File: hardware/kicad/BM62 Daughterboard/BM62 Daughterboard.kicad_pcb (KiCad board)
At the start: 2 copper layers, 29 x 34.5 mm, 10 parts, among them J1 Conn_2x4, SW1 SW_DIP_x03, U1 BM62

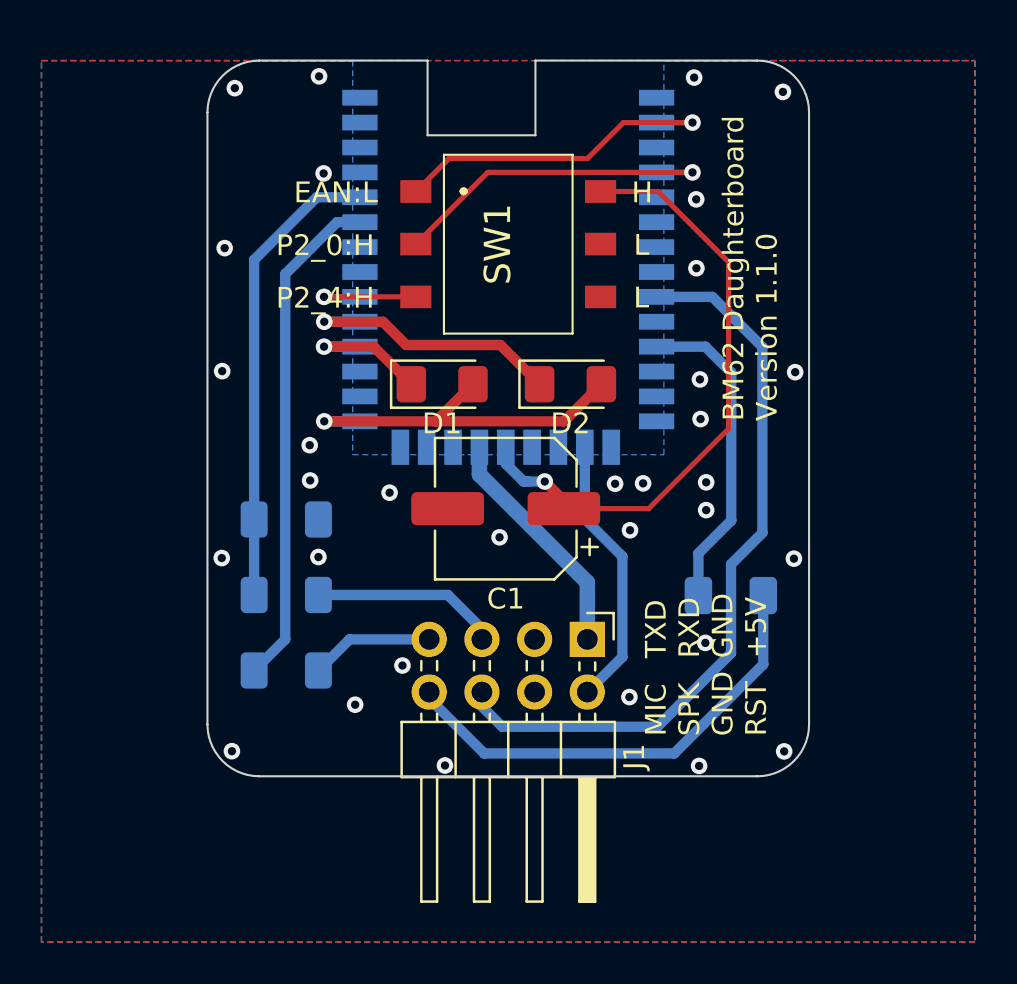
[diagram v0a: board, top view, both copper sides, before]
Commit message: Align some components better on the BM62 Daughterboard PCB
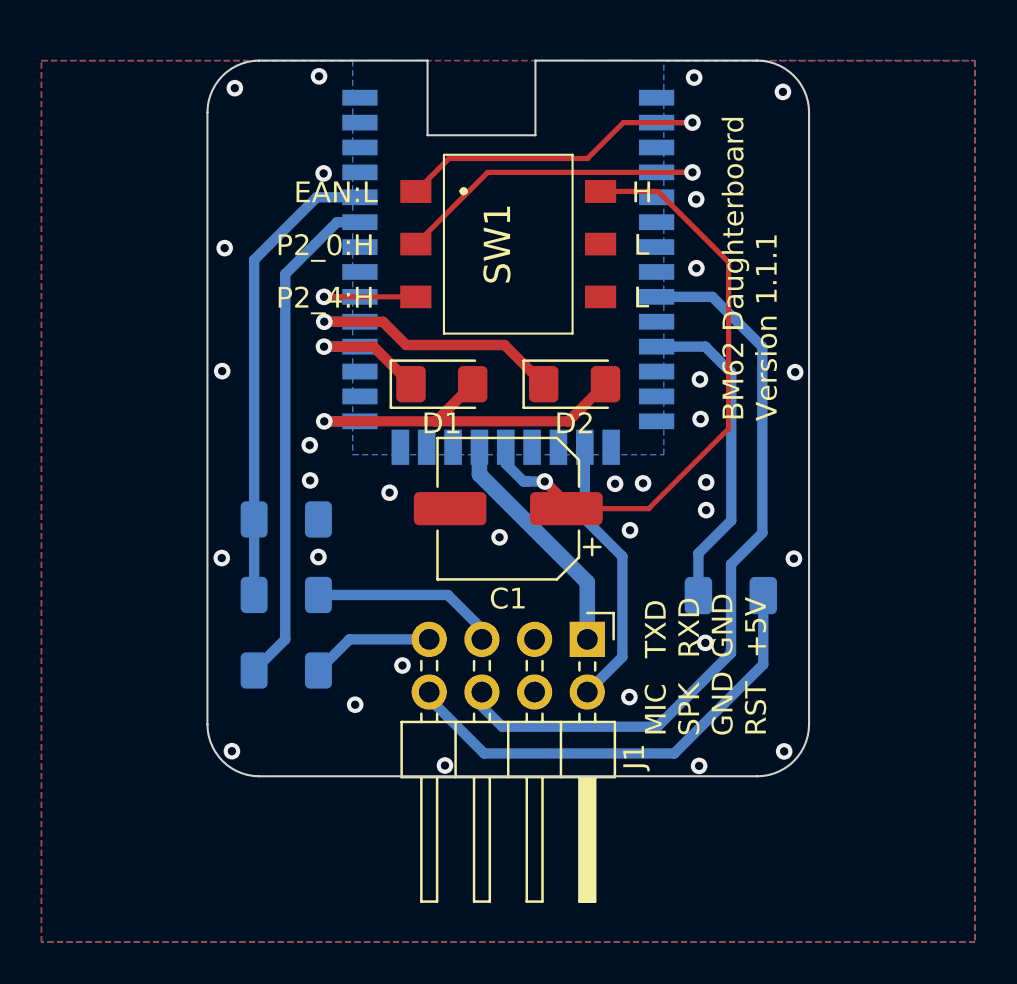
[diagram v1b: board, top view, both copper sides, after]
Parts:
- moved D2 0.20 mm to (150.7, 100.6)
- moved C1 0.12 mm to (147.5, 106.6)
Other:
- board text added: "BM62 Daughterboard Version 1.1.1"
- board text removed: "BM62 Daughterboard Version 1.1.0"
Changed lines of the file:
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@@
   (net 38 "/EAN")
   (footprint "Capacitor_SMD:CP_Elec_6.3x5.4" (layer "F.Cu")
-    (at 147.38 106.6 180)
+    (at 147.5 106.6 180)
     (descr "SMD capacitor, aluminum electrolytic, Panasonic C55, 6.3x5.4mm")
     (tags "capacitor electrolytic")
@@
   )
   (footprint "LED_SMD:LED_1206_3216Metric_Pad1.42x1.75mm_HandSolder" (layer "F.Cu")
-    (at 144.3125 100.6)
+    (at 144.2995 100.6)
     (descr "LED SMD 1206 (3216 Metric), square (rectangular) end terminal, IPC_7351 nominal, (Body size source: http://www.tortai-tech.com/upload/download/2011102023233369053.pdf), generated with kicad-footprint-generator")
     (tags "LED handsolder")
@@
   )
   (footprint "LED_SMD:LED_1206_3216Metric_Pad1.42x1.75mm_HandSolder" (layer "F.Cu")
-    (at 150.5 100.6)
+    (at 150.7 100.6)
     (descr "LED SMD 1206 (3216 Metric), square (rectangular) end terminal, IPC_7351 nominal, (Body size source: http://www.tortai-tech.com/upload/download/2011102023233369053.pdf), generated with kicad-footprint-generator")
     (tags "LED handsolder")
@@
     (effects (font (size 1 1) (thickness 0.15)) (justify left bottom))
   )
-  (gr_text "BM62 Daughterboard\nVersion 1.1.0" (at 160.56 102.38 90) (layer "F.SilkS")
+  (gr_text "BM62 Daughterboard\nVersion 1.1.1" (at 160.56 102.38 90) (layer "F.SilkS")
     (effects (font (size 1 1) (thickness 0.15)) (justify left bottom))
   )
@@
   (via (at 156.74 100.37) (size 0.8) (drill 0.4) (layers "F.Cu" "B.Cu") (free) (net 3))
   (via (at 157 113.07) (size 0.8) (drill 0.4) (layers "F.Cu" "B.Cu") (free) (net 3))
+  (segment (start 150.3 106.33) (end 150.3 106.6) (width 0.5) (layer "F.Cu") (net 4))
+  (segment (start 158.12 94.71) (end 154.72 91.31) (width 0.25) (layer "F.Cu") (net 4))
+  (segment (start 154.27 106.6) (end 158.12 102.75) (width 0.25) (layer "F.Cu") (net 4))
+  (segment (start 150.3 106.6) (end 154.27 106.6) (width 0.25) (layer "F.Cu") (net 4))
   (segment (start 158.12 102.75) (end 158.12 94.71) (width 0.25) (layer "F.Cu") (net 4))
-  (segment (start 154.27 106.6) (end 158.12 102.75) (width 0.25) (layer "F.Cu") (net 4))
-  (segment (start 150.18 106.21) (end 150.18 106.6) (width 0.5) (layer "F.Cu") (net 4))
-  (segment (start 149.26 105.29) (end 150.18 106.21) (width 0.5) (layer "F.Cu") (net 4))
-  (segment (start 158.12 94.71) (end 154.72 91.31) (width 0.25) (layer "F.Cu") (net 4))
-  (segment (start 150.18 106.6) (end 154.27 106.6) (width 0.25) (layer "F.Cu") (net 4))
+  (segment (start 149.26 105.29) (end 150.3 106.33) (width 0.5) (layer "F.Cu") (net 4))
   (segment (start 154.72 91.31) (end 151.95 91.31) (width 0.25) (layer "F.Cu") (net 4))
   (via (at 149.26 105.29) (size 0.8) (drill 0.4) (layers "F.Cu" "B.Cu") (net 4))
@@
   (segment (start 158.25 100.04) (end 157 98.79) (width 0.5) (layer "B.Cu") (net 25))
   (segment (start 156.6675 108.7525) (end 158.25 107.17) (width 0.5) (layer "B.Cu") (net 25))
-  (segment (start 142.825 100.6) (end 141.015 98.79) (width 0.5) (layer "F.Cu") (net 26))
-  (segment (start 141.015 98.79) (end 138.62 98.79) (width 0.5) (layer "F.Cu") (net 26))
+  (segment (start 141.002 98.79) (end 138.62 98.79) (width 0.5) (layer "F.Cu") (net 26))
+  (segment (start 142.812 100.6) (end 141.002 98.79) (width 0.5) (layer "F.Cu") (net 26))
   (via (at 138.62 98.79) (size 0.8) (drill 0.4) (layers "F.Cu" "B.Cu") (net 26))
   (segment (start 138.62 98.79) (end 140.35 98.79) (width 0.5) (layer "B.Cu") (net 26))
-  (segment (start 144.01 102.39) (end 145.8 100.6) (width 0.5) (layer "F.Cu") (net 27))
+  (segment (start 145.787 100.613) (end 145.787 100.6) (width 0.5) (layer "F.Cu") (net 27))
   (segment (start 138.63 102.39) (end 144.01 102.39) (width 0.5) (layer "F.Cu") (net 27))
-  (segment (start 144.01 102.39) (end 150.1975 102.39) (width 0.5) (layer "F.Cu") (net 27))
-  (segment (start 150.1975 102.39) (end 151.9875 100.6) (width 0.5) (layer "F.Cu") (net 27))
+  (segment (start 144.01 102.39) (end 150.3975 102.39) (width 0.5) (layer "F.Cu") (net 27))
+  (segment (start 144.01 102.39) (end 145.787 100.613) (width 0.5) (layer "F.Cu") (net 27))
+  (segment (start 150.3975 102.39) (end 152.1875 100.6) (width 0.5) (layer "F.Cu") (net 27))
   (via (at 138.63 102.39) (size 0.8) (drill 0.4) (layers "F.Cu" "B.Cu") (net 27))
   (segment (start 140.35 102.39) (end 138.63 102.39) (width 0.5) (layer "B.Cu") (net 27))
@@
   (segment (start 151.31 110.15) (end 146.11 104.95) (width 0.75) (layer "B.Cu") (net 28))
   (segment (start 151.31 112.9) (end 151.31 110.15) (width 0.75) (layer "B.Cu") (net 28))
+  (segment (start 142.58 98.71) (end 141.46 97.59) (width 0.5) (layer "F.Cu") (net 29))
+  (segment (start 147.3225 98.71) (end 142.58 98.71) (width 0.5) (layer "F.Cu") (net 29))
+  (segment (start 149.2125 100.6) (end 147.3225 98.71) (width 0.5) (layer "F.Cu") (net 29))
   (segment (start 141.46 97.59) (end 138.63 97.59) (width 0.5) (layer "F.Cu") (net 29))
-  (segment (start 149.0125 100.6) (end 147.1225 98.71) (width 0.5) (layer "F.Cu") (net 29))
-  (segment (start 147.1225 98.71) (end 142.58 98.71) (width 0.5) (layer "F.Cu") (net 29))
-  (segment (start 142.58 98.71) (end 141.46 97.59) (width 0.5) (layer "F.Cu") (net 29))
   (via (at 138.63 97.59) (size 0.8) (drill 0.4) (layers "F.Cu" "B.Cu") (net 29))
   (segment (start 138.63 97.59) (end 140.35 97.59) (width 0.5) (layer "B.Cu") (net 29))

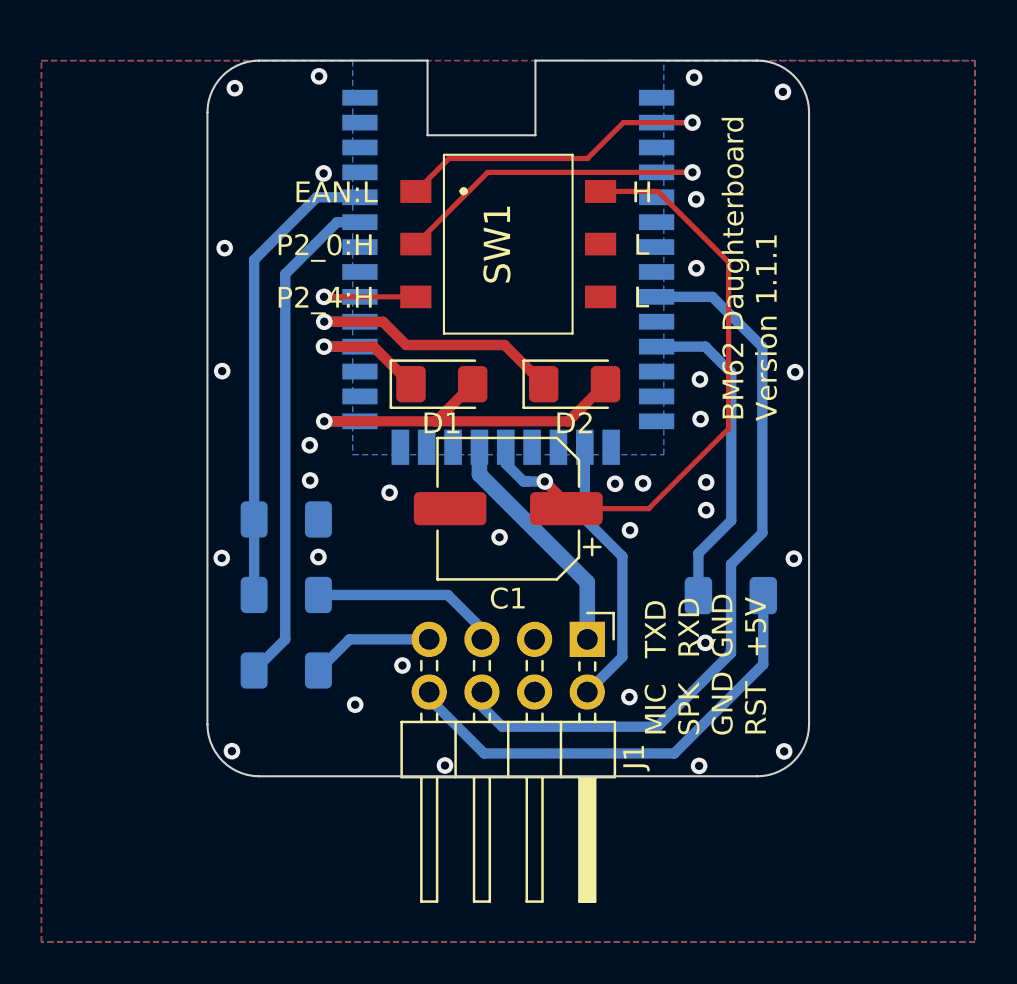
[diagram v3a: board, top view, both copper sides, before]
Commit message: BM62 Daughterboard fixes
* Fixed some pin assignments that I must have messed up previously
* Added JLCPCB part numbers for parts on the bottom side
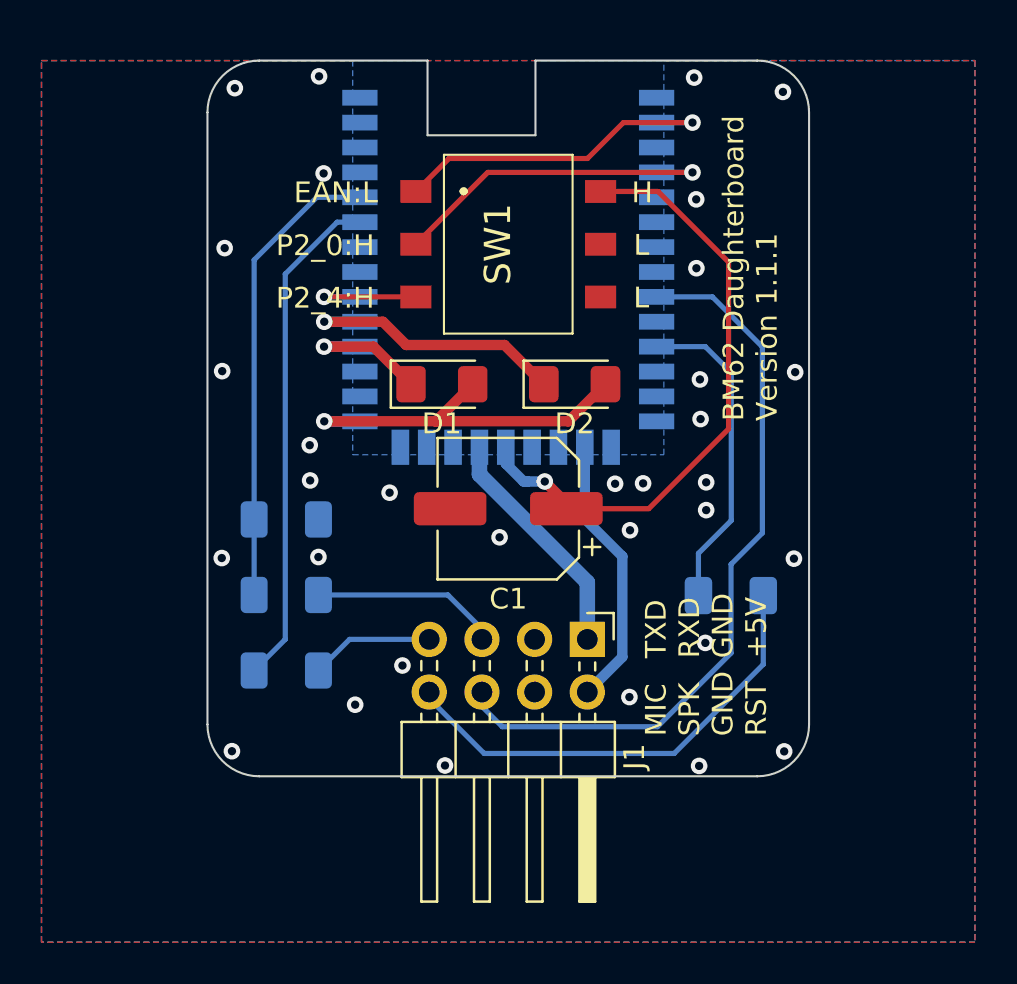
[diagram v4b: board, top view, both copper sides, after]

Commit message: Minor BM62 daughterboard PCB improvements
* Center/align some components.
* Setup proper copper exclusion in the BM62 footprint.
* Increase width of several ground connections.
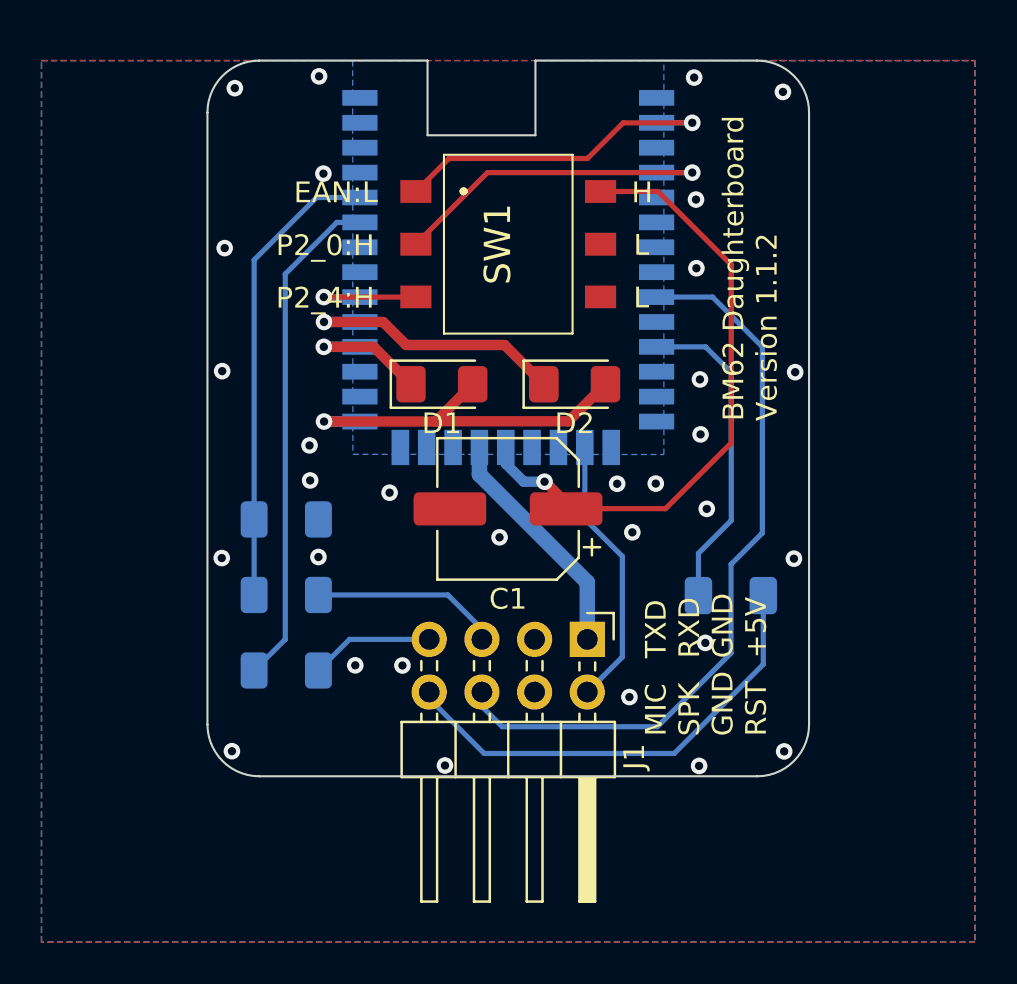
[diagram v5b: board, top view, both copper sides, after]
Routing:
- net /VDD_IO: track 29.8 -> 30.4 mm
- net GND: vias 32 -> 31
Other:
- board text added: "BM62 Daughterboard Version 1.1.2"
- board text removed: "BM62 Daughterboard Version 1.1.1"
